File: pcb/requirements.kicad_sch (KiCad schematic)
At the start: 0 parts

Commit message: Set stackup; added pics to root; minor graphics editing; fixed models
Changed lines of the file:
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@@
 		)
 	)
-	(text_box "PCB:\n2 Layers\nThickness: 1.6mm\nCopper: 1oz\nFinish: HASL\nSoldermask: Purple\nSilkscreen: White\nMin Trace: 6mil\nMin Spacing: 5mil\nMin Drill: 0.25mm\nMin Via: 0.3mm\nMin Via Annular Ring: 0.6mm\n\n"
+	(text_box "PCB:\n4 Layers\nThickness: 1.6mm\nCopper: 1oz\nFinish: HASL\nSoldermask: Purple\nSilkscreen: White\nMin Trace: 6mil\nMin Spacing: 5mil\nMin Drill: 0.25mm\nMin Via: 0.3mm\nMin Via Annular Ring: 0.6mm\n\n"
 		(exclude_from_sim yes)
 		(at 189.992 82.296 0)
@@
 		)
 	)
-	(text_box "BASIC\n\n* Detect AC current up to 30A\n* Output proportional to current\n* Analog output 0 - 3.3VDC\n"
+	(text_box "BASIC\n\n* Detect AC current up to 30A\n* Adjustable gain/sensitivity\n* VOUT proportional to current\n* Linear analog output 0 - 3.3VDC\n* AC direct connect or through cable\n* 10/3 SJTW Max\n"
 		(exclude_from_sim yes)
 		(at 17.78 25.4 0)
@@
 		)
 	)
-	(text_box "Design Considerations\n\nTBD"
+	(text_box "Design Considerations\n\n* Considerable current on AC side\n* Coupling from AC to DC\n* Transients when AC switched ON/OFF"
 		(exclude_from_sim yes)
 		(at 103.886 82.296 0)

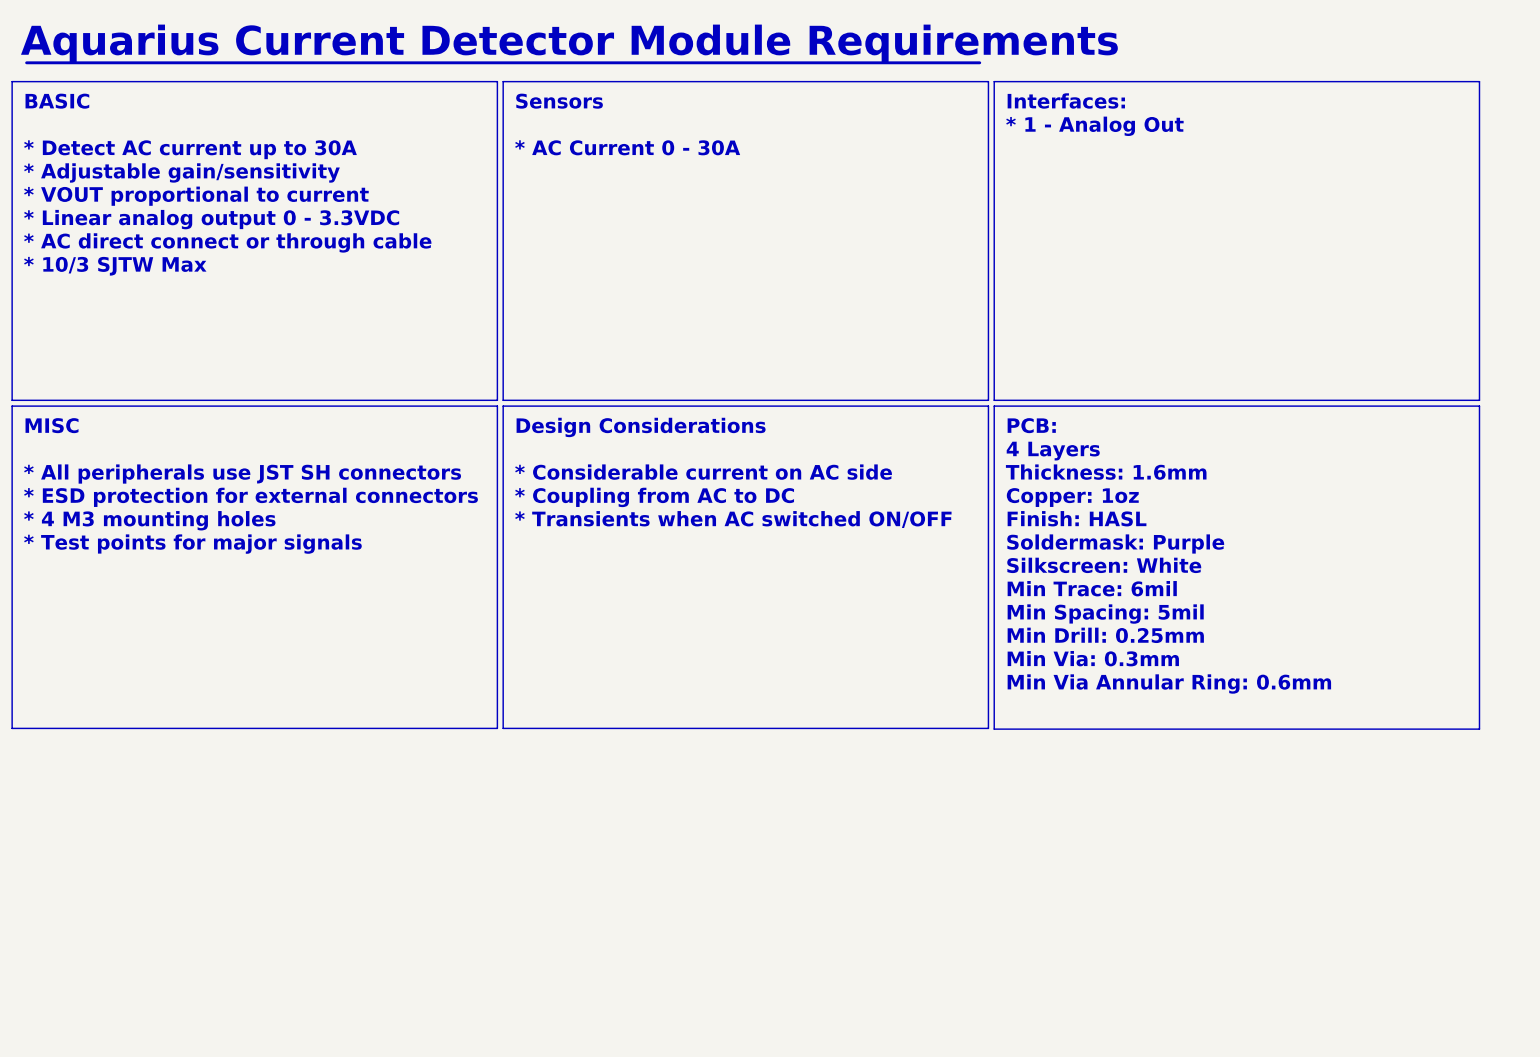
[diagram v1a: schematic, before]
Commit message: Removed CSV bom file; moved logos to symbols
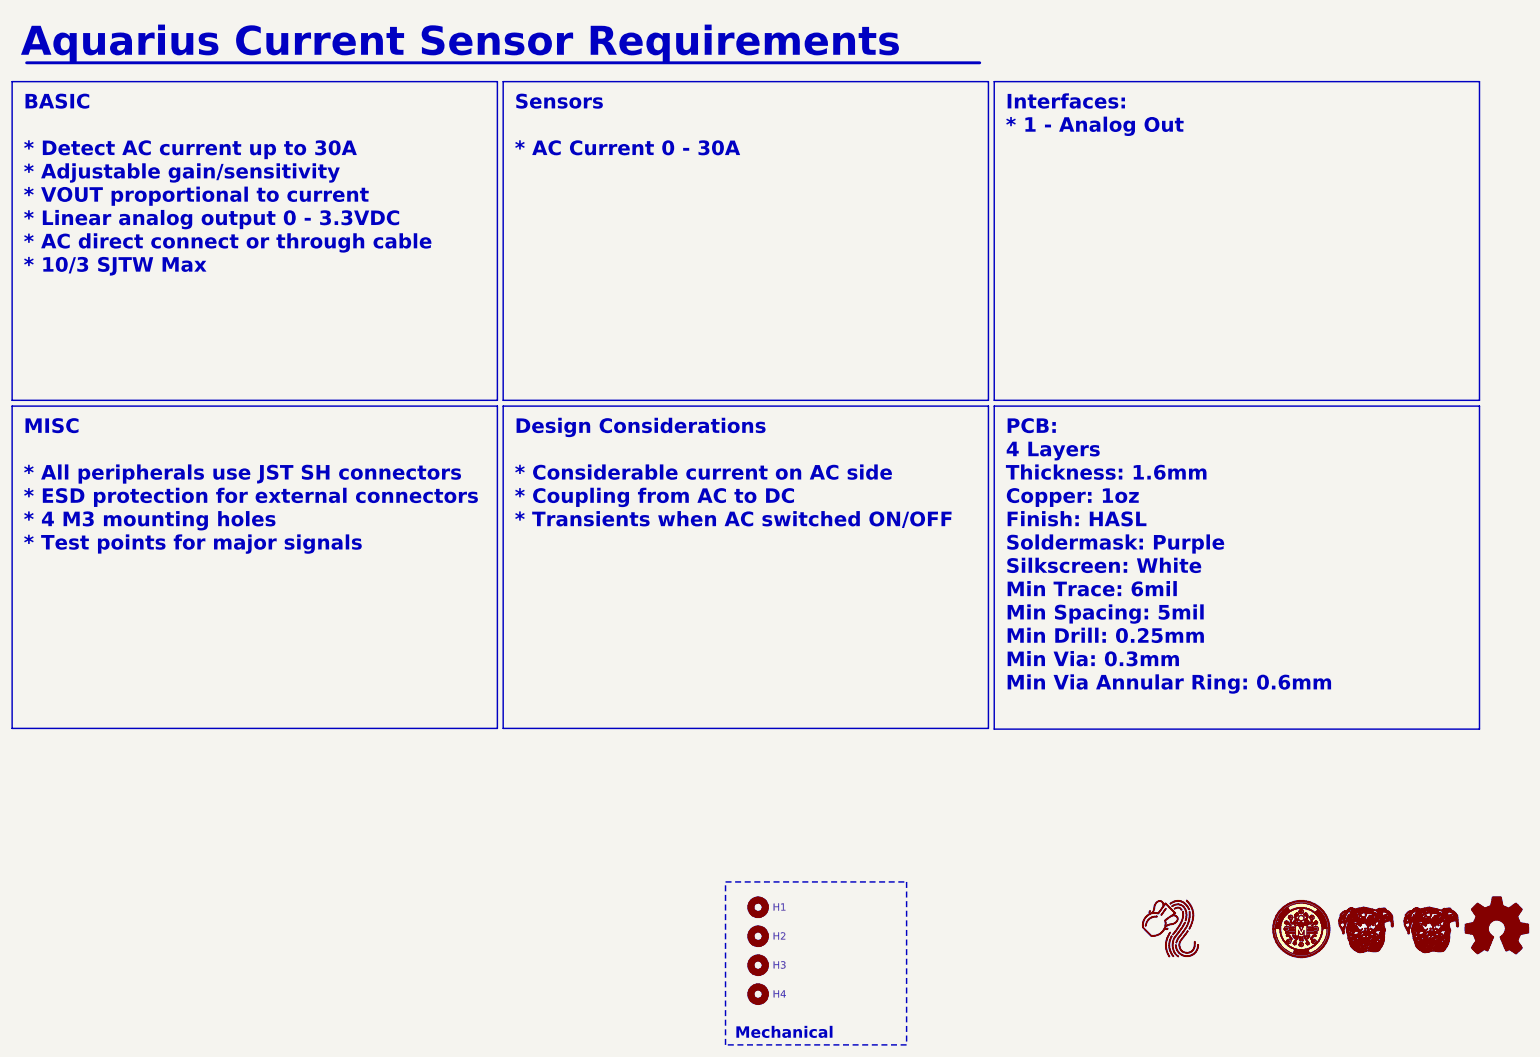
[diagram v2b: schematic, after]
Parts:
- added H1, H2, H3, H4: ~, CRGM Mechanical:MountingHole_3.2mm_M3_Pad_Via, symbol Mechanical:MountingHole
- added LOGO1: ~, CRGM Logos:CRGM Logo 7mm, symbol CRGM Logos:CRGM Logo
- added LOGO2: ~, CRGM Logos:Roxy 5mm, symbol CRGM Logos:Roxy Logo
- added LOGO3: ~, CRGM Logos:Aquarius Logo 5mm, symbol CRGM Logos:Aquarius Logo
- added LOGO4: ~, Symbol:OSHW-Logo_5.7x6mm_SilkScreen, symbol Graphic:Logo_Open_Hardware_Small
- added LOGO5: ~, CRGM Logos:Roxy 6.5mm, symbol CRGM Logos:Roxy Logo
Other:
- note added: "Aquarius Current Sensor Requirements"
- note added: "Mechanical"
- note removed: "Aquarius Current Detector Module Requirements"
- title: Current Detector -> Current Sensor
